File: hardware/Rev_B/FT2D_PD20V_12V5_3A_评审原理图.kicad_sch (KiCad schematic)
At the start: 58 parts, among them J1 USB4085-GF-A, J2 PD_PROGRAM_TEST, J3 E-DC-6_PIGTAIL, Q1 STL6P3LLH6, U1 STUSB4500QTR, U2 LM61460AASQRJRRQ1, U3 TPS259474ARPWR

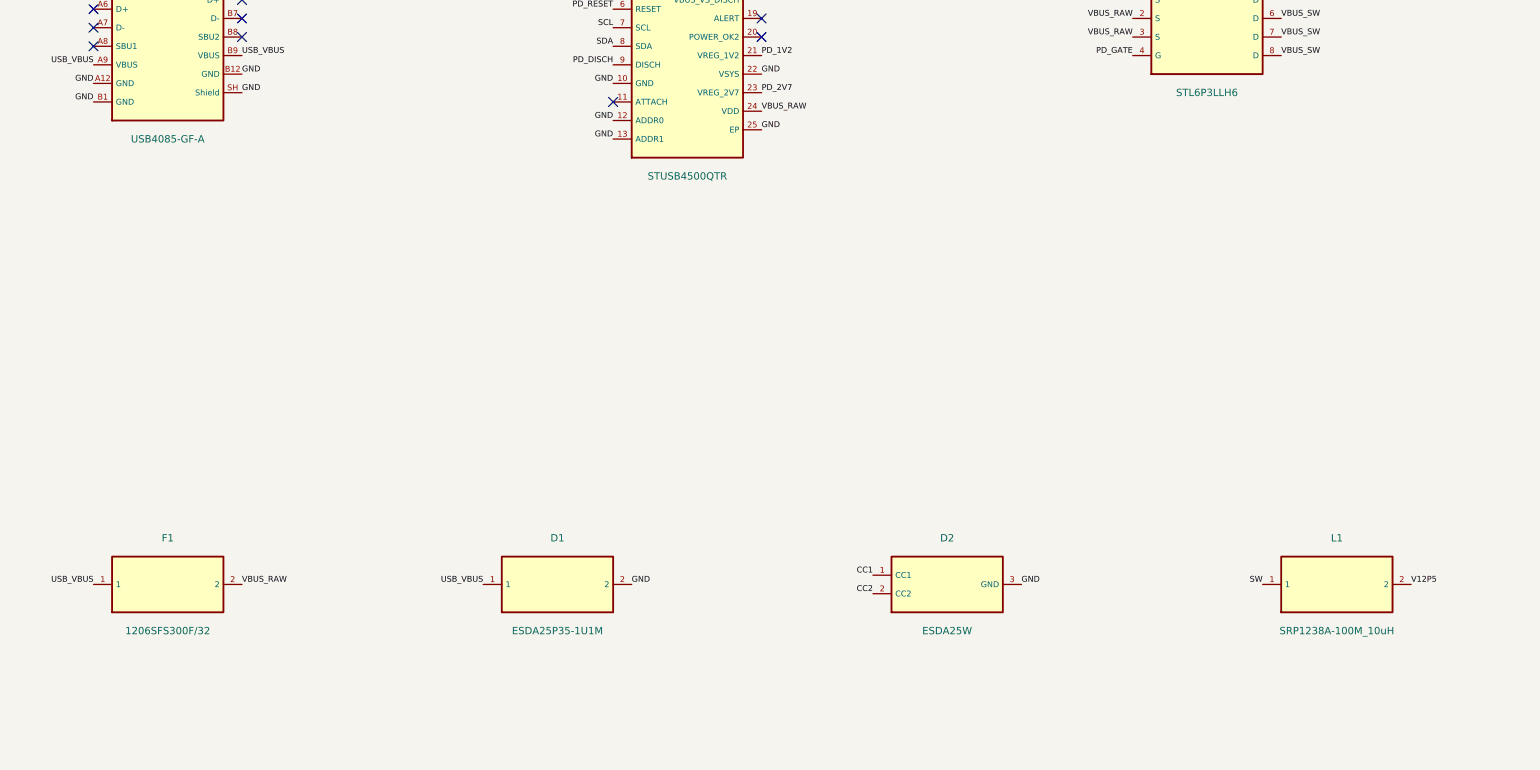
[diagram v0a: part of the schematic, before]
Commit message: Rev B: verify JLC SMT J1/L1, tighten buck routing and audit 3A/GND (NO-GO)
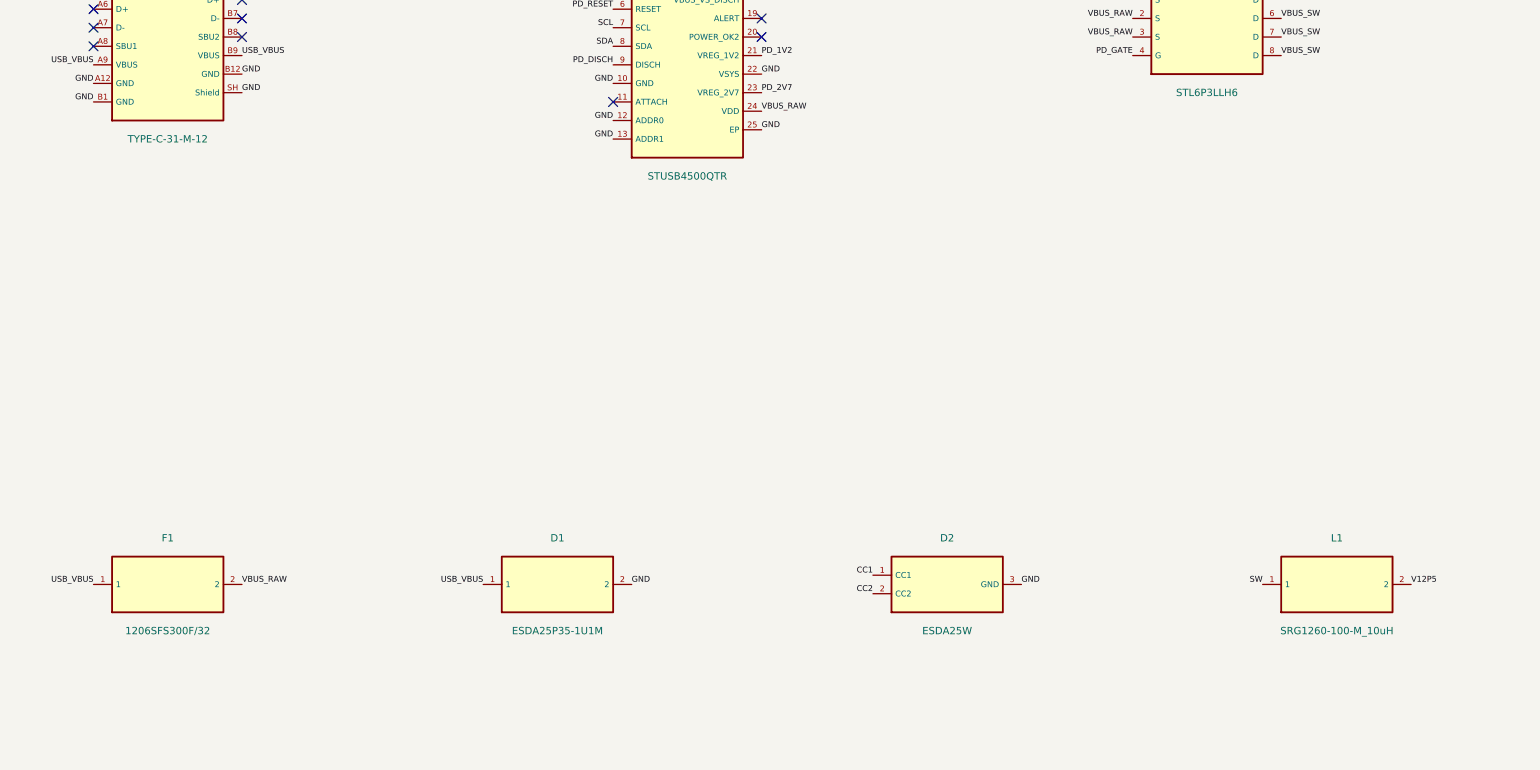
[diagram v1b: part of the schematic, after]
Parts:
- J1: value USB4085-GF-A -> TYPE-C-31-M-12; footprint Connector_USB:USB_C_Receptacle_GCT_USB4085 -> Connector_USB:USB_C_Receptacle_HRO_TYPE-C-31-M-12
- L1: value SRP1238A-100M_10uH -> SRG1260-100-M_10uH; footprint FT2D:Bourns_SRP1238A -> FT2D:JIERR_SRG1260_100M
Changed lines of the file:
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@@
     (dnp no)
     (property "Reference" "J1" (at 50.8 45.72 0) (effects (font (size 1 1))))
-    (property "Value" "USB4085-GF-A" (at 50.8 76.2 0) (effects (font (size 1 1))))
-    (property "Footprint" "Connector_USB:USB_C_Receptacle_GCT_USB4085" (at 50.8 60.96 0) (effects (font (size 1 1)) (hide yes)))
+    (property "Value" "TYPE-C-31-M-12" (at 50.8 76.2 0) (effects (font (size 1 1))))
+    (property "Footprint" "Connector_USB:USB_C_Receptacle_HRO_TYPE-C-31-M-12" (at 50.8 60.96 0) (effects (font (size 1 1)) (hide yes)))
     (property "Datasheet" "" (at 0 0 0) (effects (font (size 1 1)) (hide yes)))
     (pin "A1")
@@
     (dnp no)
     (property "Reference" "L1" (at 210.82 130.81 0) (effects (font (size 1 1))))
-    (property "Value" "SRP1238A-100M_10uH" (at 210.82 143.51 0) (effects (font (size 1 1))))
-    (property "Footprint" "FT2D:Bourns_SRP1238A" (at 210.82 137.16 0) (effects (font (size 1 1)) (hide yes)))
-    (property "Datasheet" "" (at 0 0 0) (effects (font (size 1 1)) (hide yes)))
-    (pin "1")
+    (property "Value" "SRG1260-100-M_10uH" (at 210.82 143.51 0) (effects (font (size 1 1))))
+    (property "Footprint" "FT2D:JIERR_SRG1260_100M" (at 210.82 137.16 0) (effects (font (size 1 1)) (hide yes)))
+    (property "Datasheet" "" (at 0 0 0) (effects (font (size 1 1)) (hide yes)))
+    (pin "1")

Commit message: Rev B: clear ERC/DRC/GND, validate C18 JLC hybrid footprint, export QA Gerbers and SMT sourcing review (NO-GO)
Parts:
- C18: value EEHZL1V470R_47u -> EEHZA1V470P_47u; footprint Capacitor_SMD:CP_Elec_5x5.8 -> Capacitor_SMD:CP_Elec_6.3x5.8
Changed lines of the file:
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@@
     (dnp no)
     (property "Reference" "C18" (at 530.86 245.11 0) (effects (font (size 1 1))))
-    (property "Value" "EEHZL1V470R_47u" (at 530.86 257.81 0) (effects (font (size 1 1))))
-    (property "Footprint" "Capacitor_SMD:CP_Elec_5x5.8" (at 530.86 251.46 0) (effects (font (size 1 1)) (hide yes)))
+    (property "Value" "EEHZA1V470P_47u" (at 530.86 257.81 0) (effects (font (size 1 1))))
+    (property "Footprint" "Capacitor_SMD:CP_Elec_6.3x5.8" (at 530.86 251.46 0) (effects (font (size 1 1)) (hide yes)))
     (property "Datasheet" "" (at 0 0 0) (effects (font (size 1 1)) (hide yes)))
     (pin "1")

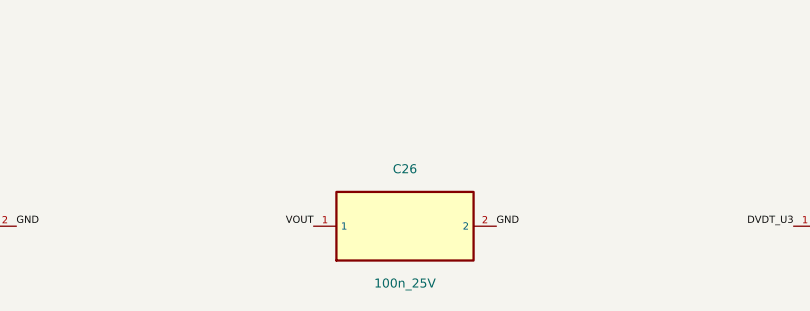
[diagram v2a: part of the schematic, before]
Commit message: Rev B: stitch U3 power copper and upgrade output bypass; refresh JLC review QA (NO-GO)
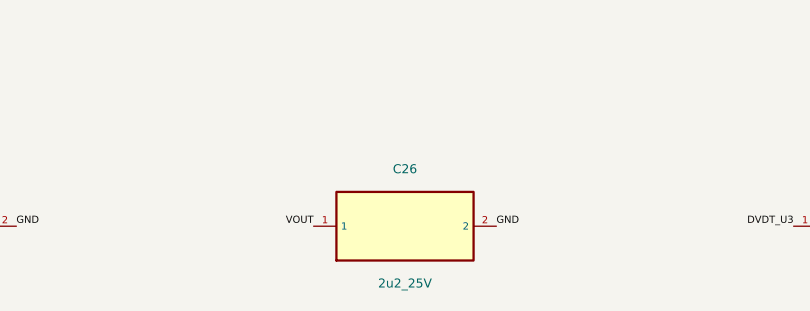
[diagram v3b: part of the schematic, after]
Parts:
- C26: value 100n_25V -> 2u2_25V
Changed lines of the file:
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@@
     (dnp no)
     (property "Reference" "C26" (at 424.18 283.21 0) (effects (font (size 1 1))))
-    (property "Value" "100n_25V" (at 424.18 295.91 0) (effects (font (size 1 1))))
+    (property "Value" "2u2_25V" (at 424.18 295.91 0) (effects (font (size 1 1))))
     (property "Footprint" "Capacitor_SMD:C_0603_1608Metric" (at 424.18 289.56 0) (effects (font (size 1 1)) (hide yes)))
     (property "Datasheet" "" (at 0 0 0) (effects (font (size 1 1)) (hide yes)))

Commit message: Rev B: qualify JLC SMT 102k OVLO resistor and refresh fab preview artifacts (NO-GO)
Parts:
- R22: value 101k -> 102k
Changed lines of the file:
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@@
     (dnp no)
     (property "Reference" "R22" (at 104.14 207.01 0) (effects (font (size 1 1))))
-    (property "Value" "101k" (at 104.14 219.71 0) (effects (font (size 1 1))))
+    (property "Value" "102k" (at 104.14 219.71 0) (effects (font (size 1 1))))
     (property "Footprint" "Resistor_SMD:R_0603_1608Metric" (at 104.14 213.36 0) (effects (font (size 1 1)) (hide yes)))
     (property "Datasheet" "" (at 0 0 0) (effects (font (size 1 1)) (hide yes)))
